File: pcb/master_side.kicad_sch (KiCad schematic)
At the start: 56 parts, among them J1 AudioJack4, J2 Conn_01x02, J3 Conn_02x18_Odd_Even, J4 Conn_02x18_Odd_Even, J5 USB_C_Receptacle_USB2.0_14P, Q1 Q_NMOS, SW1 RotaryEncoder, SW2 SW_Push, U1 W25Q128JVS, U2 NCP1117-3.3_SOT223, U3 RP2040, U4 OPT3001DNPR, Y1 ABM8-272-T3

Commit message: Restructure file & folder layout
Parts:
- removed Q1: Q_NMOS, symbol Device:Q_NMOS
- added F2: Polyfuse_Small, symbol Device:Polyfuse_Small
- added R14: 0, Resistor_SMD:R_1210_3225Metric_Pad1.30x2.65mm_HandSolder, symbol library:R
- added U5: PCA9956BTWY, PCA9956BTWY:SOP50P640X110-39N, symbol PCA9956BTWY:PCA9956BTWY
- C1, C10, C11, C12, C13, C14, C15, C16, C4, C5, C6, C7, C8, C9: footprint Capacitor_SMD:C_0402_1005Metric -> Capacitor_SMD:C_0805_2012Metric
- C18: footprint (none) -> Capacitor_SMD:C_0805_2012Metric
- R10, R11, R12, R13, R6, R7, R8, R9: footprint (none) -> Resistor_SMD:R_0402_1005Metric
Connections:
- net +5V: now also R14.1, U5.38 (VDD); no longer J1.T
- net GND: now also U5.14 (VSS), U5.18 (VSS), U5.2 (AD0), U5.21 (VSS), U5.25 (VSS), U5.3 (AD1), U5.34 (VSS), U5.39 (EXP), U5.4 (AD2)
- net GPIO2: now also U5.37 (SDA)
- net GPIO3: now also U5.36 (SCL)
- new net: F2.1, R14.2
- new net: F2.2, J1.T
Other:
- note added: "EXP is the heatsink under the IC, make many thermal vias under the chip"
- note added: "I2C: 0000001"
- note added: "I2C: 1000100"
- moved on the sheet: C1, C10, C11, C12, C13, C14, C15, C16, C18, C2, C3, C4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

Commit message: feat: Add more components, add finalized outline
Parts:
- removed U1: W25Q128JVS, W25Q128JVSIQ:SOIC127P790X216-8N, symbol library:W25Q128JVS
- removed U2: NCP1117-3.3_SOT223, Package_TO_SOT_SMD:SOT-223-3_TabPin2, symbol Regulator_Linear:NCP1117-3.3_SOT223
- added J7: 54-00174, 54-00174:TENSILITY_54-00174, symbol 54-00174:54-00174
- added U2: W25Q128JVSIQ, W25Q128JVSIQ:SOIC127P790X216-8N, symbol W25Q128JVSIQ:W25Q128JVSIQ
- added U6: NCP1117LPST33T3G, NCP1117LPST33T3G:SOT230P700X175-4N, symbol NCP1117LPST33T3G:NCP1117LPST33T3G
- J1: footprint (none) -> Connector_Audio:Plug_3.5mm_CUI_SP-3541
- J5: footprint (none) -> Connector_USB:USB_C_Receptacle_GCT_USB4085
- R14: footprint Resistor_SMD:R_1210_3225Metric_Pad1.30x2.65mm_HandSolder -> Resistor_SMD:R_0805_2012Metric_Pad1.20x1.40mm_HandSolder
- U4: footprint Package_TO_SOT_SMD:SOT-223-3_TabPin2 -> OPT3001DNPR:SON65P200X200X65-7N
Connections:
- net +3V3: now also U2.8 (VCC), U6.2 (OUTPUT), U6.4 (OUTPUT__1)
- net +5V: now also U6.3 (INPUT)
- net GND: now also U2.4 (GND), U6.1 (GND)
- net QSPI_SCLK: now also U2.6 (CLK)
- net QSPI_SD0: now also U2.5 (DI(IO0))
- net QSPI_SD1: now also U2.2 (DO(IO1))
- net QSPI_SD2: now also U2.3 (/WP(IO2))
- net QSPI_SD3: now also U2.7 (/HOLD/RESET(IO3))
- net QSPI_SS: now also U2.1 (/CS)
- net ~{USB_BOOT}: no longer J2.1 (Pin_1), R2.2
- new net: J2.1 (Pin_1), R2.2
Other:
- moved on the sheet: C1, C10, C11, C12, C13, C14, C15, C16, C18, C2, C3, C4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

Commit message: feat: Add both sides of outline in CAD
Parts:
- removed C17: 10u, Capacitor_SMD:C_0805_2012Metric, symbol library:C
- removed J3, J4: Conn_02x18_Odd_Even, Connector_PinHeader_2.54mm:PinHeader_2x18_P2.54mm_Vertical, symbol library:Conn_02x18_Odd_Even
- removed SW1: RotaryEncoder, symbol Device:RotaryEncoder
- removed SW2: SW_Push, symbol Switch:SW_Push
- added D1, D2, D3, D4, D5, D6, D7, D9: LED_Small, symbol Device:LED_Small
- added SW1: SW_SPDT, symbol Switch:SW_SPDT
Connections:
- net +5V: now also D1.1 (K), D2.1 (K), D3.1 (K), D4.1 (K), D5.1 (K), D6.1 (K), D7.1 (K), D9.1 (K)
- net GND: now also SW1.2 (B)
- net GPIO6: now also SW1.1 (A)
- net GPIO7: now also SW1.3 (C)
- net at U5.10 (LED4): now also D3.2 (A)
- net at U5.11 (LED5): now also D2.2 (A)
- net at U5.12 (LED6): now also D1.2 (A)
- net at U5.13 (LED7): now also D9.2 (A)
- net at U5.6 (LED0): now also D7.2 (A)
- net at U5.7 (LED1): now also D6.2 (A)
- net at U5.8 (LED2): now also D5.2 (A)
- net at U5.9 (LED3): now also D4.2 (A)
- net GPIO8: no longer names the net of U3.11 (GPIO8)
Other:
- note added: "Enable internal pull-up on GPIO6 and 7"
- note removed: "IOs"
- note removed: "volume knob"

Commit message: feat: Further develop right side
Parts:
- removed C3: 10u, Capacitor_SMD:C_0805_2012Metric, symbol Device:C
- removed D1, D2, D3, D4, D5, D6, D7, D9: LED_Small, symbol Device:LED_Small
- removed H1, H2, H3, H4: MountingHole, MountingHole:MountingHole_2.7mm_M2.5, symbol library:MountingHole
- removed J1: AudioJack4, Connector_Audio:Plug_3.5mm_CUI_SP-3541, symbol Connector_Audio:AudioJack4
- removed J7: 54-00174, 54-00174:TENSILITY_54-00174, symbol 54-00174:54-00174
- removed R1: DNF, Resistor_SMD:R_0402_1005Metric, symbol library:R
- removed SW1: SW_SPDT, symbol Switch:SW_SPDT
- removed TP3: TestPoint, symbol Connector:TestPoint
- removed U6: NCP1117LPST33T3G, NCP1117LPST33T3G:SOT230P700X175-4N, symbol NCP1117LPST33T3G:NCP1117LPST33T3G
- added C17: 10u, Capacitor_SMD:C_0805_2012Metric, symbol Device:C
- added D10, D11, D12, D13, D14, D15, D16, D17, D18, D19, D20, D3, D4, D5, D6, D7, D8, D9: D_Small, symbol Device:D_Small
- added D21: LED_Small, symbol Device:LED_Small
- added J3: 4P4C_Shielded, Connector_RJ:RJ9_Evercom_5301-440xxx_Horizontal, symbol Connector:4P4C_Shielded
- added SW10, SW11, SW12, SW13, SW14, SW15, SW16, SW17, SW18, SW19, SW2, SW3, SW4, SW5, SW6, SW7, SW8, SW9: SW_Push_45deg, ai03-MX_V2:MX-Solderable-1U, symbol Switch:SW_Push_45deg
- added SW38: SW_SPDT_MSM, symbol Switch:SW_SPDT_MSM
- added TP4, TP6, TP7: TestPoint, TestPoint:TestPoint_Pad_D2.0mm, symbol Connector:TestPoint
- added U3: NCP1117LPST33T3G, NCP1117LPST33T3G:SOT230P700X175-4N, symbol NCP1117LPST33T3G:NCP1117LPST33T3G
- TP1: renamed from TP2; footprint (none) -> TestPoint:TestPoint_Pad_D2.0mm
- TP2: renamed from TP1; footprint (none) -> TestPoint:TestPoint_Pad_D2.0mm
- TP3: renamed from TP4; footprint (none) -> TestPoint:TestPoint_Pad_D2.0mm
- TP5: footprint (none) -> TestPoint:TestPoint_Pad_D2.0mm
- renumbered C9 to C1, C8 to C11, C1 to C12, C2 to C13, C4 to C14, C5 to C15, C18 to C16, C11 to C2, C12 to C3, C13 to C4, C14 to C5, C15 to C6, C16 to C7, C6 to C8, C7 to C9, D2 to D1, D1 to D2, J5 to J1, R4 to R1, R13 to R10, R12 to R11, R9 to R12, R8 to R13, R5 to R2, R6 to R3, R7 to R4, R2 to R5, R14 to R6, R3 to R7, R10 to R8, R11 to R9, U2 to U1, U3 to U2
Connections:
- net QSPI_SS is gone; now on net +3V3: R5.1, U1.1 (/CS), U2.56 (QSPI_SS)
- net +3V3: now also U5.38 (VDD), C17.1, TP7.1, U3.2 (OUTPUT), U3.4 (OUTPUT__1)
- net +5V: now also D21.2 (A), U3.3 (INPUT); no longer U5.38 (VDD)
- net GND: now also C17.2, J3.2, SW38.2 (3), U3.1 (GND)
- net GPIO0: now also J3.4
- net GPIO1: now also J3.3
- net GPIO6: now also SW38.1
- net GPIO7: now also SW38.3 (4)
- net ROW1: now reaches U2.11 (GPIO8)
- net ROW1: now also D3.1 (K), D4.1 (K), D5.1 (K), D6.1 (K), D7.1 (K), D8.1 (K)
- net ROW2: now reaches U2.12 (GPIO9)
- net ROW2: now also D10.1 (K), D11.1 (K), D12.1 (K), D13.1 (K), D14.1 (K), D9.1 (K)
- net ROW3: now reaches U2.13 (GPIO10)
- net ROW3: now also D15.1 (K), D16.1 (K), D17.1 (K), D18.1 (K), D19.1 (K), D20.1 (K)
- net COL1: now reaches U2.14 (GPIO11)
- net COL1: now also SW14.1, SW2.1, SW8.1
- net COL2: now reaches U2.15 (GPIO12)
- net COL2: now also SW15.1, SW3.1, SW9.1
- net COL3: now reaches U2.16 (GPIO13)
- net COL3: now also SW10.1, SW16.1, SW4.1
- net COL4: now reaches U2.17 (GPIO14)
- net COL4: now also SW11.1, SW17.1, SW5.1
- net COL5: now reaches U2.18 (GPIO15)
- net COL5: now also SW12.1, SW18.1, SW6.1
- net at U2.24 (SWCLK): now also TP4.1
- net at U2.25 (SWD): now also TP6.1
- net COL6: now reaches U2.27 (GPIO16)
- net COL6: now also SW13.1, SW19.1, SW7.1
- net at U5.6 (LED0): now also D21.1 (K)
- net at F2.2: now also J3.1
- new net: D12.2 (A), SW11.2
- new net: D4.2 (A), SW3.2
- new net: D14.2 (A), SW13.2
- new net: D5.2 (A), SW4.2
- new net: D6.2 (A), SW5.2
- new net: D17.2 (A), SW16.2
- new net: D18.2 (A), SW17.2
- new net: D3.2 (A), SW2.2
- new net: D10.2 (A), SW9.2
- new net: D19.2 (A), SW18.2
- new net: D8.2 (A), SW7.2
- new net: D7.2 (A), SW6.2
- new net: D16.2 (A), SW15.2
- new net: D13.2 (A), SW12.2
- new net: D9.2 (A), SW8.2
- new net: D11.2 (A), SW10.2
- new net: D20.2 (A), SW19.2
- new net: D15.2 (A), SW14.2
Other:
- moved on the sheet: C12, R5

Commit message: fix: left/right nets separation
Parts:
- removed D21: LED_Small, symbol Device:LED_Small
- removed R10, R11: 33, Resistor_SMD:R_0402_1005Metric, symbol library:R
- removed U5: PCA9956BTWY, PCA9956BTWY:SOP50P640X110-39N, symbol PCA9956BTWY:PCA9956BTWY
- added D15: LED_Small, symbol Device:LED_Small
- added IC1: PCA9956BTWY, HTSSOP38_4P4X9P7_NXP, symbol 2026-03-25_16-41-27:PCA9956BTWY
- added R3, R5: 10k, symbol Device:R_Small
- renumbered D15 to D16, D16 to D17, D17 to D18, D18 to D19, D19 to D20, D20 to D21, R8 to R10, R9 to R11, R3 to R4, R4 to R6, R5 to R7, R6 to R8, R7 to R9, SW38 to SW1
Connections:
- net +3V3: now also IC1.38 (VDD)
- net +5V: now also D15.2 (A)
- net GND: now also IC1.14 (VSS), IC1.18 (VSS), IC1.2 (AD0), IC1.21 (VSS), IC1.25 (VSS), IC1.3 (AD1), IC1.34 (VSS), IC1.4 (AD2)
- net GPIO0: now also R3.2; no longer U2.2 (GPIO0)
- net GPIO1: now also R5.2; no longer U2.3 (GPIO1)
- net GPIO2: now also R10.2, U4.6 (SDA), IC1.37 (SDA)
- net GPIO3: now also R11.2, U4.4 (SCL), IC1.36 (SCL)
- new net: R3.1, U2.2 (GPIO0)
- new net: R5.1, U2.3 (GPIO1)
- new net: D15.1 (K), IC1.6 (LED0)

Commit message: feat: Replace PCA9555 with MCP23017
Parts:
- IC1: footprint HTSSOP38_4P4X9P7_NXP -> PCA9956BTWY:HTSSOP38_4P4X9P7_NXP
- R3, R5: footprint (none) -> Resistor_SMD:R_0402_1005Metric
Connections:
- net GND: now also IC1.5 (OE), IC1.EPAD, J3.SH, U4.7 (EXP)
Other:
- note added: "exposed thermal pad"
- note added: "thermal pad under IC"
- note removed: "do not connect"
- moved on the sheet: R3

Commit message: fix: I2C pullups on both buses
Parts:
- removed R10, R11: 3.3k, Resistor_SMD:R_0402_1005Metric, symbol library:R
- removed R8: 0, Resistor_SMD:R_0805_2012Metric_Pad1.20x1.40mm_HandSolder, symbol library:R
- removed SW1: SW_SPDT_MSM, symbol Switch:SW_SPDT_MSM
- removed TP5: TestPoint, TestPoint:TestPoint_Pad_D2.0mm, symbol Connector:TestPoint
- added R4: 2.2k, symbol Device:R_Small
- added R6: 4.7k, symbol Device:R_Small
- added SW1: SW_SP3T, symbol Switch:SW_SP3T
- R3: value 10k -> 2.2k; footprint Resistor_SMD:R_0402_1005Metric -> (none)
- R5: value 10k -> 4.7k; footprint Resistor_SMD:R_0402_1005Metric -> (none)
- renumbered D9 to D10, D10 to D11, D11 to D12, D12 to D13, D13 to D14, D14 to D15, D15 to D9, R9 to R10, R12 to R11, R13 to R12, R4 to R7, R6 to R8, R7 to R9, TP6 to TP5, TP7 to TP6
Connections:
- net +3V3: now also R3.1, R5.1, R4.1, R6.1
- net +5V: now also F2.1
- net COL1: now also U2.15 (GPIO12); no longer U2.14 (GPIO11)
- net COL2: now also U2.16 (GPIO13); no longer U2.15 (GPIO12)
- net COL3: now also U2.17 (GPIO14); no longer U2.16 (GPIO13)
- net COL4: now also U2.18 (GPIO15); no longer U2.17 (GPIO14)
- net COL5: now also U2.27 (GPIO16); no longer U2.18 (GPIO15)
- net COL6: now also U2.28 (GPIO17); no longer U2.27 (GPIO16)
- net GND: now also SW1.3
- net GPIO0: now also U2.2 (GPIO0)
- net GPIO1: now also U2.3 (GPIO1), R4.2; no longer R5.2
- net GPIO2: now also R5.2
- net GPIO3: now also R6.2
- net GPIO6: now also SW1.1
- net GPIO7: now also SW1.2
- net ROW1: now also U2.12 (GPIO9); no longer U2.11 (GPIO8)
- net ROW2: now also U2.13 (GPIO10); no longer U2.12 (GPIO9)
- net ROW3: now also U2.14 (GPIO11); no longer U2.13 (GPIO10)
- new net GPIO8: SW1.4, U2.11 (GPIO8)
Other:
- note added: "Enable internal pull-up on GPIO6, 7 and 8"
- note added: "I2C pullups"
- note added: "Switch to change backlight mode in firmware"
- note added: "red LED"
- note added: "white LED"
- note removed: "Enable internal pull-up on GPIO6 and 7"
- moved on the sheet: F2, IC1, J1, R1, R2

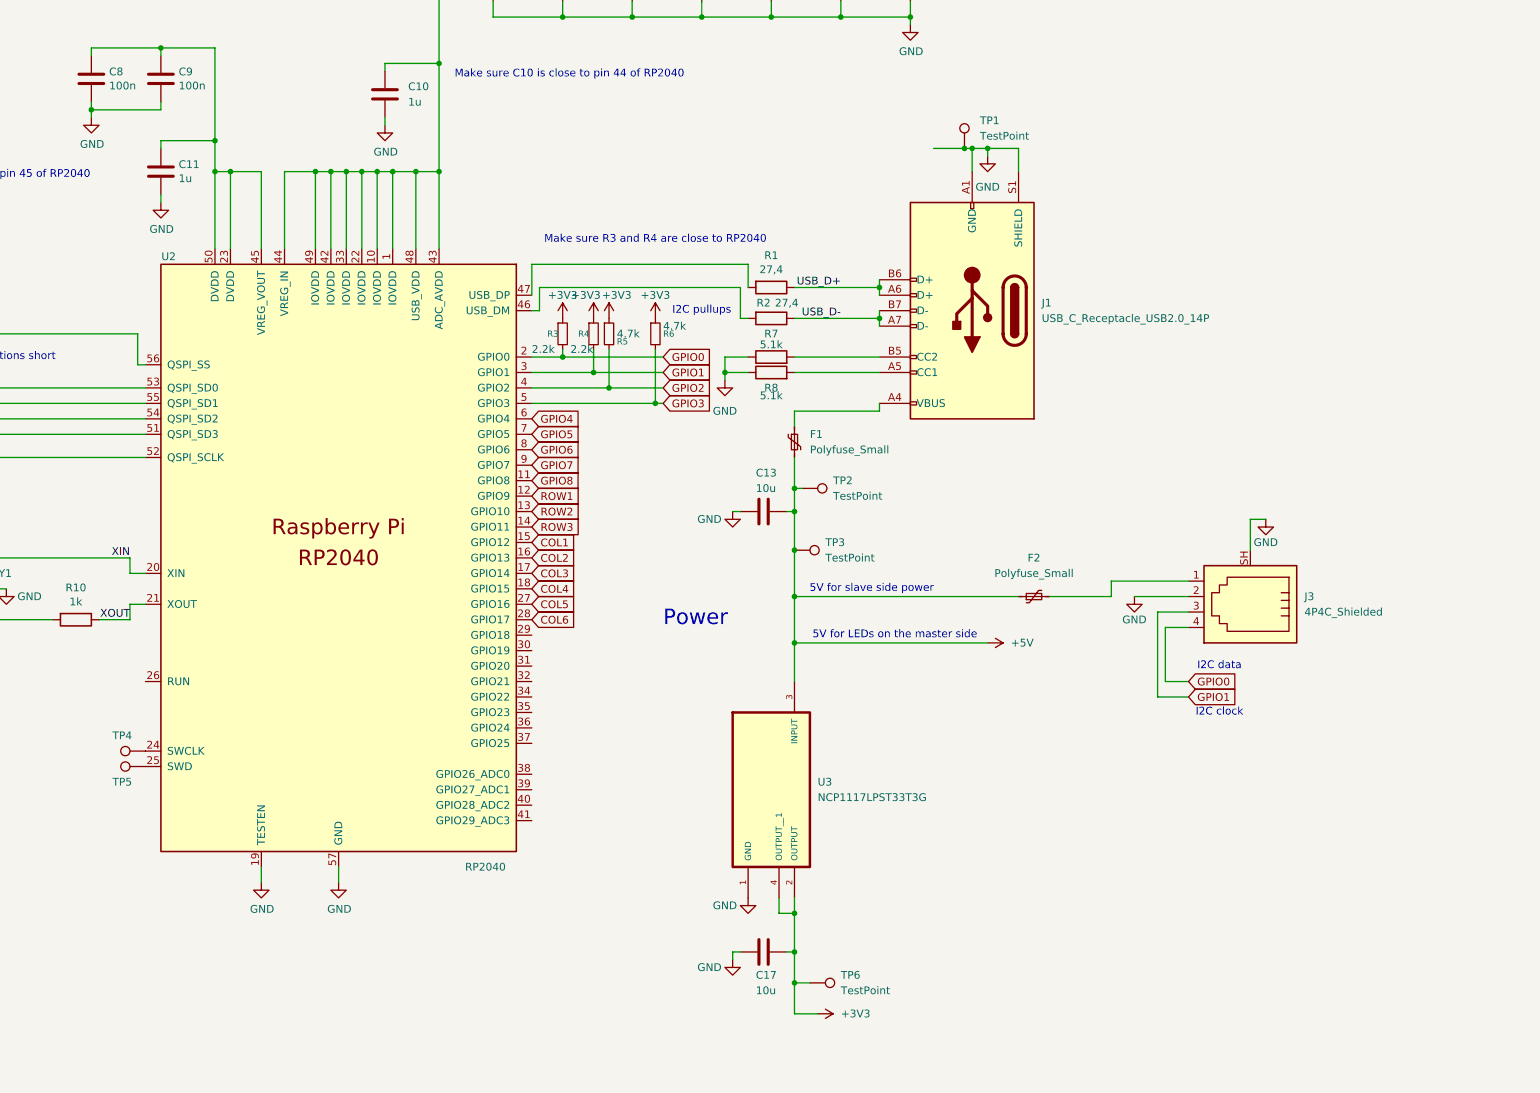
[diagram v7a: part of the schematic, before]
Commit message: fix: Proper MX LED footprint
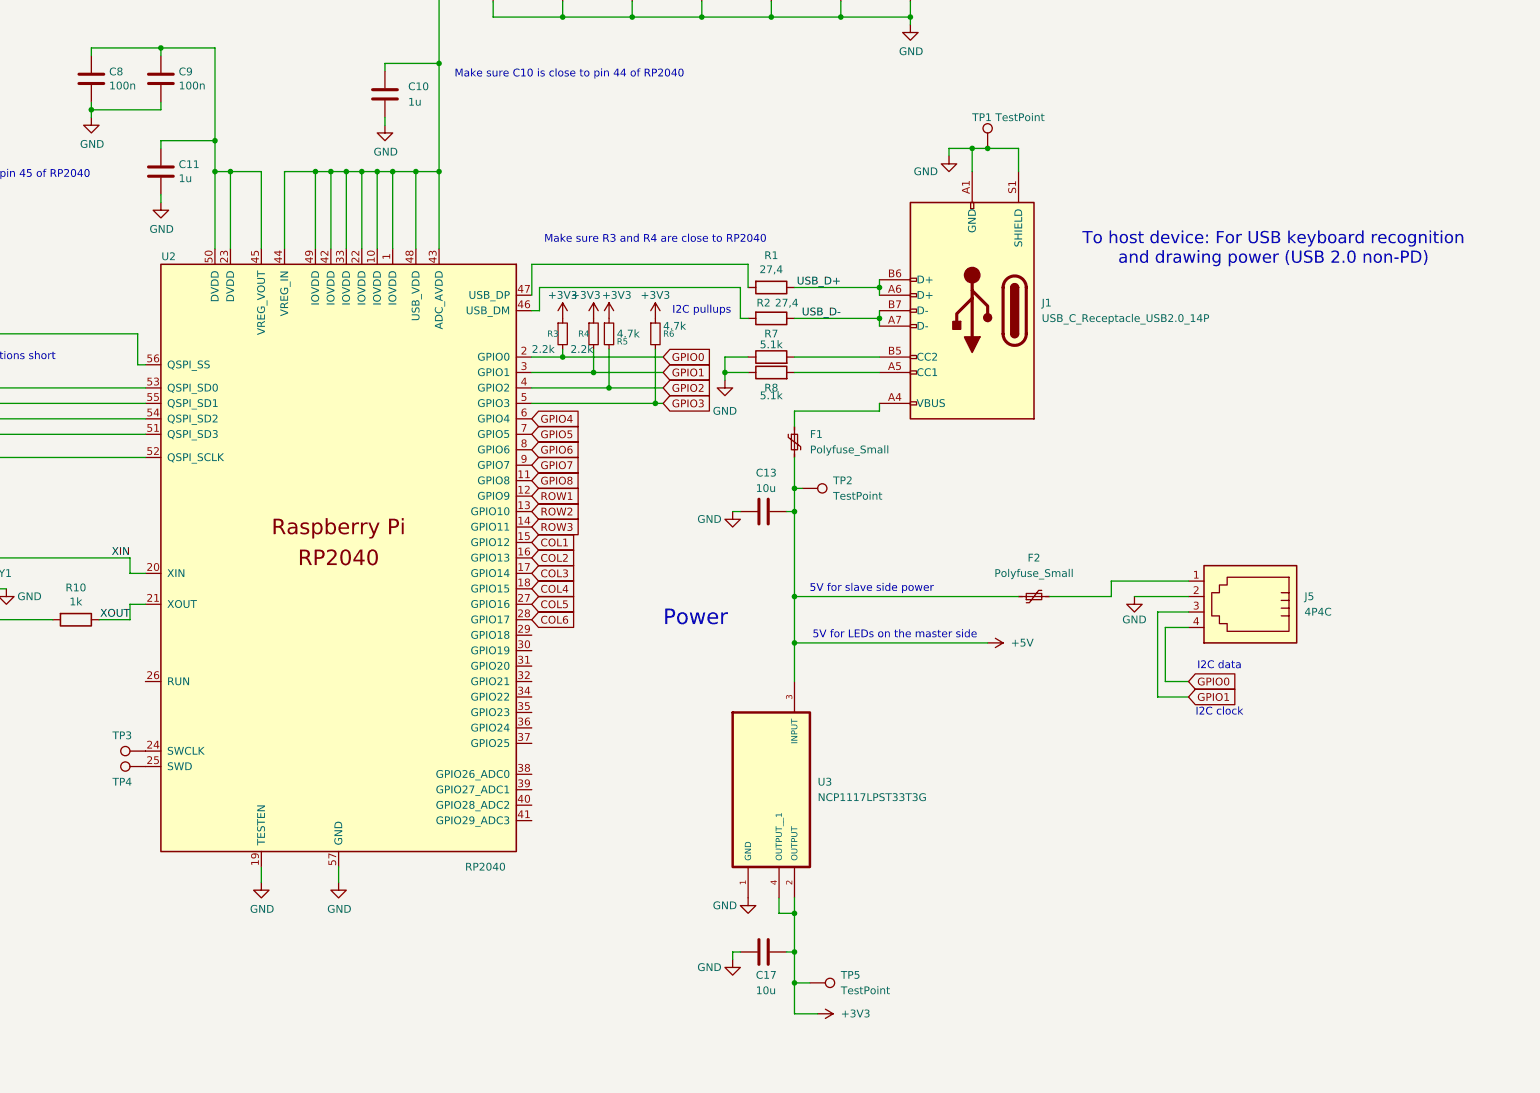
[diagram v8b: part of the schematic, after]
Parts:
- removed J3: 4P4C_Shielded, Connector_RJ:RJ9_Evercom_5301-440xxx_Horizontal, symbol Connector:4P4C_Shielded
- removed TP1: TestPoint, TestPoint:TestPoint_Pad_D2.0mm, symbol Connector:TestPoint
- added J5: 4P4C, Connector_RJ:RJ9_Evercom_5301-440xxx_Horizontal, symbol Connector:4P4C
- SW10, SW11, SW12, SW13, SW14, SW15, SW16, SW17, SW18, SW19, SW2, SW3, SW4, SW5, SW6, SW7, SW8, SW9: footprint ai03-MX_V2:MX-Solderable-1U -> ai03-MX_V2:MX-LED
- renumbered TP3 to TP1, TP4 to TP3, TP5 to TP4, TP6 to TP5
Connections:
- net +5V: no longer TP1.1
- net GND: now also TP1.1, J5.2
- net GPIO0: now also J5.4
- net GPIO1: now also J5.3
- net at F2.2: now also J5.1
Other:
- note added: "To host device: For USB keyboard recognition and drawing power (USB 2.0 non-PD)"
- moved on the sheet: TP1
